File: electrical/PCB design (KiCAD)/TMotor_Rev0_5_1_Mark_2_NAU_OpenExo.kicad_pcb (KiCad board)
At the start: 2 copper layers, 89.3 x 79.4 mm, 85 parts, among them J1 Conn_01x07_Pin, J10 XT30PW-F, J11 XT30PW-F, J12 XT30PW-F, J2 Conn_01x04_Pin, J3 Conn_01x02_Pin, J4 Conn_01x02_Pin, J5 Conn_01x02_Pin, J6 Conn_01x02_Pin, J7 Conn_01x03_Pin, J8 XT30PW-F, J9 XT30PW-F, U1 TXU0104PWR, U10 DEV-16771, U2 TXU0304-Q1, U3 INA125U, U4 INA125U, U5 SN65HVD230DR, U6 INA125U, U7 INA125U

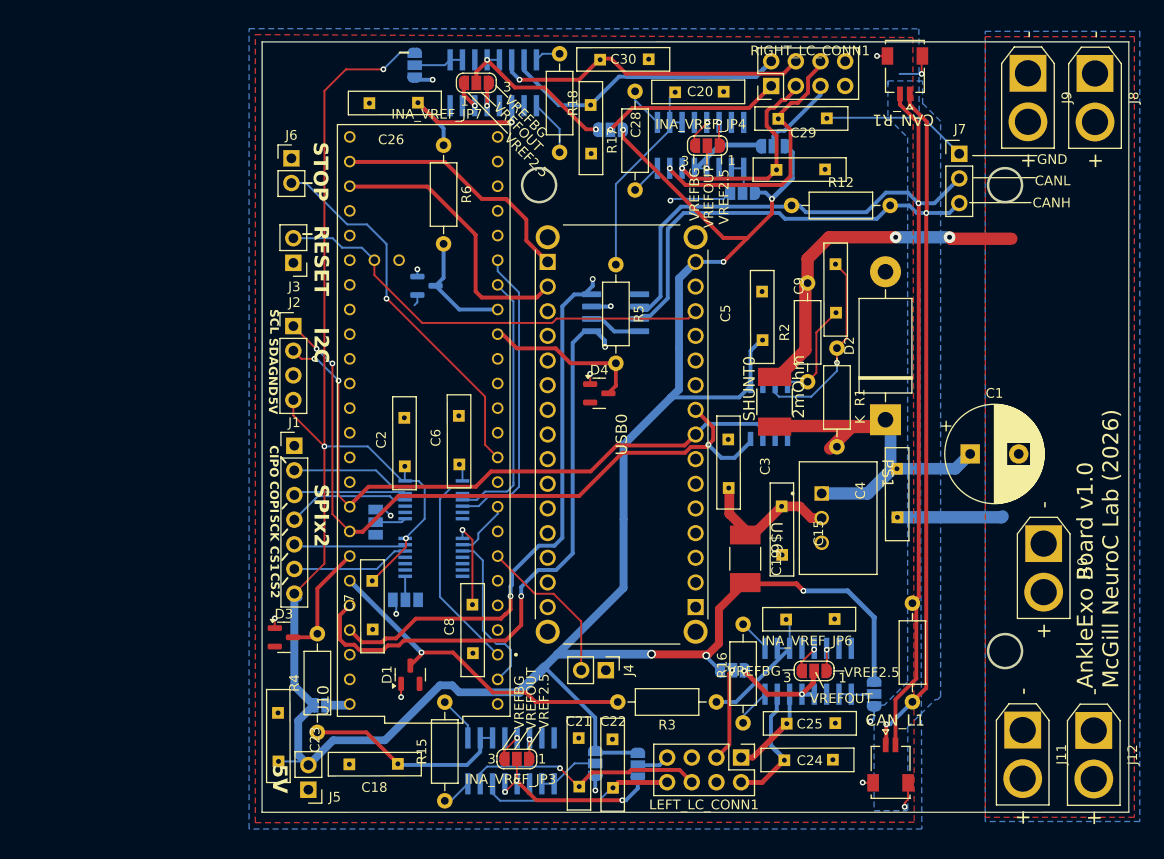
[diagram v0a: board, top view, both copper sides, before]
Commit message: documentation update for my 10 days leave ; documentation for first time teensy setup on Arduino IDE ;  SW revamp to use HW versioning conditional compiling
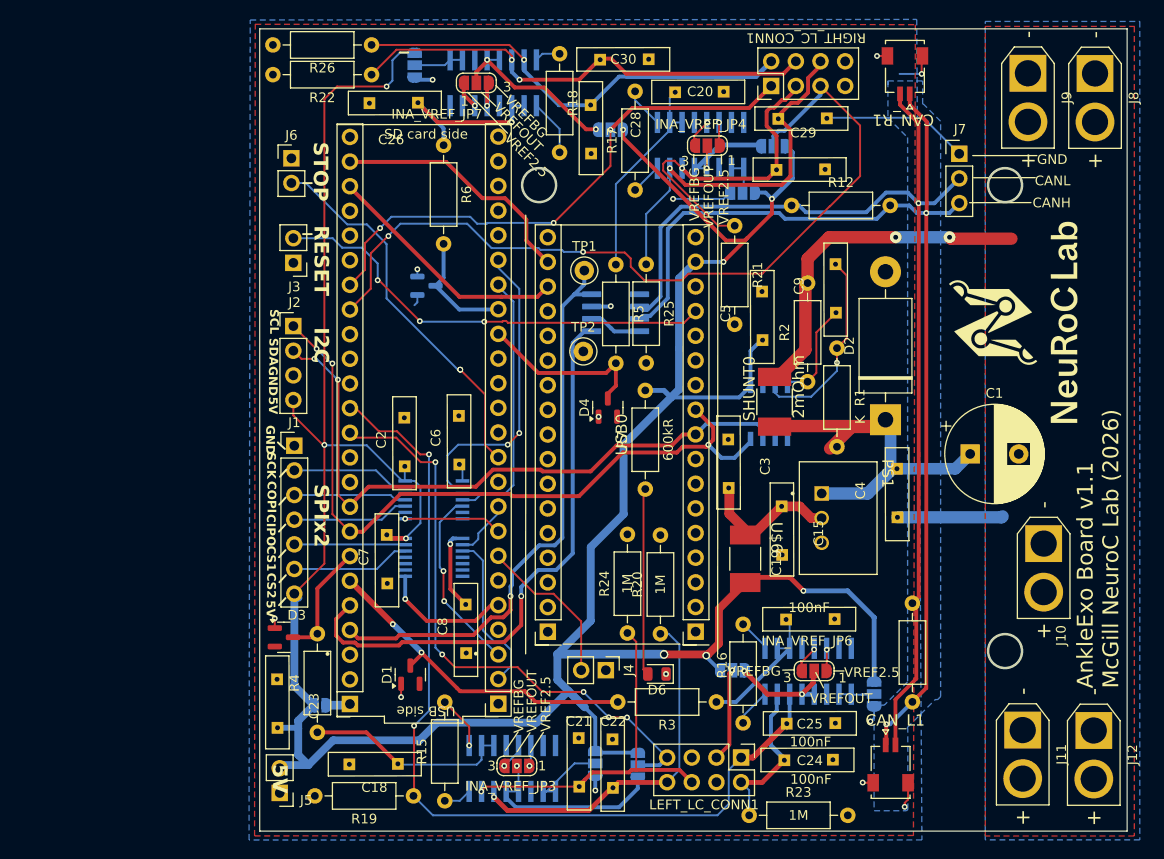
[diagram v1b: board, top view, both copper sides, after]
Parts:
- removed CSVoltageShifterOEJP1, SPIVoltageShifterOEJP1: SolderJumper_3_Open, Jumper:SolderJumper-3_P1.3mm_Open_Pad1.0x1.5mm
- added D6: LED, LED_SMD:LED_0805_2012Metric, F.Cu at (144.3, 130.4)
- added R19: 1M, Resistor_THT:R_Axial_DIN0207_L6.3mm_D2.5mm_P10.16mm_Horizontal, F.Cu at (119.2, 143.0)
- added R20: 1M, Resistor_THT:R_Axial_DIN0207_L6.3mm_D2.5mm_P10.16mm_Horizontal, F.Cu at (144.7, 126.3)
- added R21: 1M, Resistor_THT:R_Axial_DIN0207_L6.3mm_D2.5mm_P10.16mm_Horizontal, F.Cu at (152.3, 84.3)
- added R22: 1M, Resistor_THT:R_Axial_DIN0207_L6.3mm_D2.5mm_P10.16mm_Horizontal, F.Cu at (114.9, 68.7)
- added R23: 1M, Resistor_THT:R_Axial_DIN0207_L6.3mm_D2.5mm_P10.16mm_Horizontal, F.Cu at (153.8, 145.0)
- added R24: 1M, Resistor_THT:R_Axial_DIN0207_L6.3mm_D2.5mm_P10.16mm_Horizontal, F.Cu at (141.3, 126.2)
- added R25: 1M, Resistor_THT:R_Axial_DIN0207_L6.3mm_D2.5mm_P10.16mm_Horizontal, F.Cu at (143.2, 88.2)
- added R26: 1M, Resistor_THT:R_Axial_DIN0207_L6.3mm_D2.5mm_P10.16mm_Horizontal, F.Cu at (114.9, 65.6)
- added R7: 600kR, Resistor_THT:R_Axial_DIN0207_L6.3mm_D2.5mm_P10.16mm_Horizontal, F.Cu at (143.1, 111.4)
- added TP1: TestPoint, TestPoint:TestPoint_Keystone_5000-5004_Miniature, F.Cu at (136.8, 88.9)
- added TP2: TestPoint, TestPoint:TestPoint_Keystone_5000-5004_Miniature, F.Cu at (136.8, 97.2)
- G***: moved to F.Cu
- R15, R16, R17, R18: value 470R -> 10R
- moved G*** 45.7 mm to (181.4, 94.3)
- moved C7 4.97 mm to (116.5, 120.8)
- moved C23 3.47 mm to (105.3, 131.2)
- moved J5 2.97 mm to (105.5, 142.7)
- moved D4 1.72 mm to (139.3, 103.0), turned to 90 degrees
- moved U3 0.80 mm to (129.4, 140.2)
- moved INA_VREF_JP3 0.71 mm to (129.9, 139.9)
- moved C8 0.70 mm to (124.6, 128.0)
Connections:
- net Net-(J1-Pin_2) renamed /MCUs/SCK_5v
- C25 pad 1: /Load cells/Left LC Amplifier 2/Vbridge+ -> LEFT_AMP2_EXC
- INA_EXC_JP3 pad 2: /Load cells/Left LC  Amplifier 1/Vexcitation+ -> LEFT_AMP1_EXC
- INA_EXC_JP4 pad 2: /Load cells/Right LC  Amplifier 2/Vexcitation+ -> RIGHT_AMP2_EXC
- INA_EXC_JP7 pad 2: /Load cells/Right LC Amplifier 1/Vexcitation+ -> RIGHT_AMP1_EXC
- J1 pad 3: Net-(J1-Pin_3) -> /MCUs/COPI_5v
- J1 pad 4: Net-(J1-Pin_4) -> /MCUs/CIPO_5v
- LEFT_LC_CONN1 pad 1: /Load cells/Left LC Amplifier 2/Vbridge+ -> LEFT_AMP2_EXC
- LEFT_LC_CONN1 pad 7: /Load cells/Left LC  Amplifier 1/Vexcitation+ -> LEFT_AMP1_EXC
- RIGHT_LC_CONN1 pad 1: /Load cells/Right LC Amplifier 1/Vexcitation+ -> RIGHT_AMP1_EXC
- RIGHT_LC_CONN1 pad 5: /Load cells/Right LC  Amplifier 2/Vexcitation+ -> RIGHT_AMP2_EXC
- U1 pad 8: Net-(CSVoltageShifterOEJP1-C) -> /MCUs/OE2
- U10 pad 14: unconnected-(U10-A0-Pad14) -> LEFT_AMP2_EXC
- U10 pad 15: unconnected-(U10-A1-Pad15) -> LEFT_AMP1_EXC
- U10 pad 3: unconnected-(U10-LRCLK2-Pad3) -> /MCUs/OE2
- U10 pad 39: unconnected-(U10-A15-Pad39) -> RIGHT_AMP1_EXC
- U10 pad 40: unconnected-(U10-A16-Pad40) -> RIGHT_AMP2_EXC
- U10 pad 6: unconnected-(U10-OUT1D-Pad6) -> /MCUs/OE1
- U2 pad 10: unconnected-(U2-B4-Pad10) -> /MCUs/CIPO_5v
- U2 pad 11: Net-(J1-Pin_4) -> /MCUs/COPI_5v
- U2 pad 12: Net-(J1-Pin_3) -> unconnected-(U2-B2Y-Pad12)
- U2 pad 2: CIPO -> SCK1
- U2 pad 5: SCK1 -> CIPO
- U2 pad 8: Net-(SPIVoltageShifterOEJP1-C) -> /MCUs/OE1
- U6 pad 6: /Load cells/Left LC Amplifier 2/Vbridge+ -> LEFT_AMP2_EXC
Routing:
- net LEFT_AMP2_EXC: track 0.00 -> 95.0 mm, vias 0 -> 2
- net RIGHT_AMP2_EXC: track 0.00 -> 85.5 mm, vias 0 -> 2
- net LEFT_AMP1_EXC: track 0.00 -> 61.1 mm, vias 0 -> 5
- net RIGHT_AMP1_EXC: track 0.00 -> 56.4 mm, vias 0 -> 3
- net Net-(D6-A): track 0.00 -> 19.3 mm
- net /Load cells/Right LC Amplifier 1/Vexcitation+: track 18.4 -> 0.00 mm, vias 1 -> 0
- net /Load cells/Right LC Amplifier 1/Vbridge-: track 30.2 -> 46.5 mm, vias 0 -> 1
- net /Load cells/Right LC Amplifier 1/Vbridge+: track 33.0 -> 49.1 mm, vias 1 -> 2
- net /Load cells/Left LC  Amplifier 1/Vbridge+: track 21.5 -> 37.3 mm, vias 0 -> 1
- net /MCUs/OE2: track 0.00 -> 13.6 mm, vias 0 -> 1
- net /Load cells/Right LC  Amplifier 2/Vbridge+: track 21.4 -> 34.3 mm
- net Net-(J1-Pin_4): track 12.8 -> 0.00 mm
- net /Load cells/Left LC  Amplifier 1/Vbridge-: track 26.2 -> 38.7 mm
- net /MCUs/COPI_5v: track 0.00 -> 12.1 mm
- net /MCUs/CIPO_5v: track 0.00 -> 12.0 mm
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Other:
- board size 89.3 x 79.4 mm -> 89.4 x 82.6 mm
- board text added: "AnkleExo Board v1.1 McGill NeuroC Lab (2026)"
- board text removed: "AnkleExo Board v1.0 McGill NeuroC Lab (2026)"

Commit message: some modifications on the kicad
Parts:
- moved G*** 0.77 mm to (180.6, 94.3)
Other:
- board text added: "AnkleExo Board v1.0.1 McGill NeuroC Lab (2026)"
- board text removed: "AnkleExo Board v1.1 McGill NeuroC Lab (2026)"

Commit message: kicad update
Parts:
- added J13: TFM-107-01-L-D-WT, ISDF connector:SAMTEC_TFM-107-01-L-D-WT, F.Cu at (86.5, 123.1)

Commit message: PCB version v1.1.0 design+documentation
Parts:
- removed J13: TFM-107-01-L-D-WT, ISDF connector:SAMTEC_TFM-107-01-L-D-WT
- removed USB0: ABX00028, TMotor_Rev0_5_1_Mark_2_NAU_OpenExo:ABX00028
- added A1: Arduino_Nano_33_BLE_Sense_R2_Socket, PCM_arduino-library:Arduino_Nano_Every_Socket, F.Cu at (140.7, 127.4)
- moved D3 36.4 mm to (139.6, 113.1)
- moved R4 30.4 mm to (139.5, 133.3), turned to 0 degrees
- moved D1 23.5 mm to (140.6, 121.3), turned to -90 degrees
- moved R3 20.1 mm to (167.1, 122.0)
- moved LEFT_LC_CONN1 8.03 mm to (145.4, 141.6), turned to 90 degrees
- moved D4 1.59 mm to (138.5, 101.6)
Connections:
- C25 pad 1: LEFT_AMP2_EXC -> /Load cells/Left LC Amplifier 2/Vbridge+
- D1 pad 3: LEFT_LC_AMP2 -> L2_LC_N
- D3 pad 3: LEFT_LC_AMP1 -> L1_LC_N
- D4 pad 3: RIGHT_LC_AMP2 -> R2_LC_N
- D5 pad 3: RIGHT_LC_AMP1 -> R1_LC_N
- INA_EXC_JP3 pad 2: LEFT_AMP1_EXC -> L1_LC_P
- INA_EXC_JP4 pad 2: RIGHT_AMP2_EXC -> R2_LC_P
- INA_EXC_JP6 pad 2: /Load cells/Left LC Amplifier 2/Vexcitation+ -> L2_LC_P
- INA_EXC_JP7 pad 2: RIGHT_AMP1_EXC -> R1_LC_P
- LEFT_LC_CONN1 pad 1: LEFT_AMP2_EXC -> /Load cells/Left LC Amplifier 2/Vbridge+
- LEFT_LC_CONN1 pad 2: /Load cells/Left LC Amplifier 2/Vbridge- -> GND
- LEFT_LC_CONN1 pad 3: /Load cells/Left LC Amplifier 2/Vexcitation+ -> /Load cells/Left LC Amplifier 2/Vbridge-
- LEFT_LC_CONN1 pad 4: GND -> +5V
- LEFT_LC_CONN1 pad 5: GND -> +5V
- LEFT_LC_CONN1 pad 7: LEFT_AMP1_EXC -> GND
- R19 pad 1: LEFT_AMP2_EXC -> /Load cells/Left LC Amplifier 2/Vbridge+
- R3 pad 2: LEFT_LC_AMP2 -> L2_LC_N
- R4 pad 2: LEFT_LC_AMP1 -> L1_LC_N
- R5 pad 2: RIGHT_LC_AMP2 -> R2_LC_N
- R6 pad 2: RIGHT_LC_AMP1 -> R1_LC_N
- RIGHT_LC_CONN1 pad 1: RIGHT_AMP1_EXC -> /Load cells/Right LC  Amplifier 2/Vbridge+
- RIGHT_LC_CONN1 pad 2: /Load cells/Right LC Amplifier 1/Vbridge- -> GND
- RIGHT_LC_CONN1 pad 3: /Load cells/Right LC  Amplifier 2/Vbridge+ -> /Load cells/Right LC  Amplifier 2/Vbridge-
- RIGHT_LC_CONN1 pad 4: /Load cells/Right LC Amplifier 1/Vbridge+ -> +5V
- RIGHT_LC_CONN1 pad 5: RIGHT_AMP2_EXC -> +5V
- RIGHT_LC_CONN1 pad 6: /Load cells/Right LC  Amplifier 2/Vbridge- -> /Load cells/Right LC Amplifier 1/Vbridge-
- RIGHT_LC_CONN1 pad 8: GND -> /Load cells/Right LC Amplifier 1/Vbridge+
- U10 pad 14: LEFT_AMP2_EXC -> unconnected-(U10-A0-Pad14)
- U10 pad 15: LEFT_AMP1_EXC -> unconnected-(U10-A1-Pad15)
- U10 pad 18: SDA -> unconnected-(U10-A4-Pad18)
- U10 pad 19: SCL -> unconnected-(U10-A5-Pad19)
- U10 pad 20: LEFT_LC_AMP1 -> unconnected-(U10-A6-Pad20)
- U10 pad 21: LEFT_LC_AMP2 -> unconnected-(U10-A7-Pad21)
- U10 pad 24: RIGHT_LC_AMP2 -> unconnected-(U10-A10-Pad24)
- U10 pad 25: RIGHT_LC_AMP1 -> unconnected-(U10-A11-Pad25)
- U10 pad 39: RIGHT_AMP1_EXC -> unconnected-(U10-A15-Pad39)
- U10 pad 40: RIGHT_AMP2_EXC -> unconnected-(U10-A16-Pad40)
- U6 pad 6: LEFT_AMP2_EXC -> /Load cells/Left LC Amplifier 2/Vbridge+
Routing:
- net LEFT_AMP2_EXC: track 95.0 -> 0.00 mm, vias 2 -> 0
- net RIGHT_AMP2_EXC: track 85.5 -> 0.00 mm, vias 2 -> 0
- net LEFT_AMP1_EXC: track 61.1 -> 0.00 mm, vias 5 -> 0
- net R1_LC_P: track 0.00 -> 58.8 mm, vias 0 -> 3
- net RIGHT_AMP1_EXC: track 56.4 -> 0.00 mm, vias 3 -> 0
- net /Load cells/Left LC Amplifier 2/Vbridge+: track 0.00 -> 51.7 mm
- net R2_LC_P: track 0.00 -> 50.2 mm, vias 0 -> 1
- net R1_LC_N: track 0.00 -> 42.7 mm, vias 0 -> 1
- net L1_LC_P: track 0.00 -> 36.6 mm, vias 0 -> 3
- net L1_LC_N: track 0.00 -> 35.7 mm, vias 0 -> 2
- net LEFT_LC_AMP2: track 34.6 -> 0.00 mm, vias 2 -> 0
- net L2_LC_P: track 0.00 -> 31.5 mm
- net +5V: track 315.7 -> 343.3 mm
- net L2_LC_N: track 0.00 -> 26.1 mm, vias 0 -> 1
- net RIGHT_LC_AMP2: track 17.8 -> 0.00 mm
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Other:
- board text added: "AnkleExo Board v1.1.0 McGill NeuroC Lab (2026)"
- board text removed: "AnkleExo Board v1.0.1 McGill NeuroC Lab (2026)"

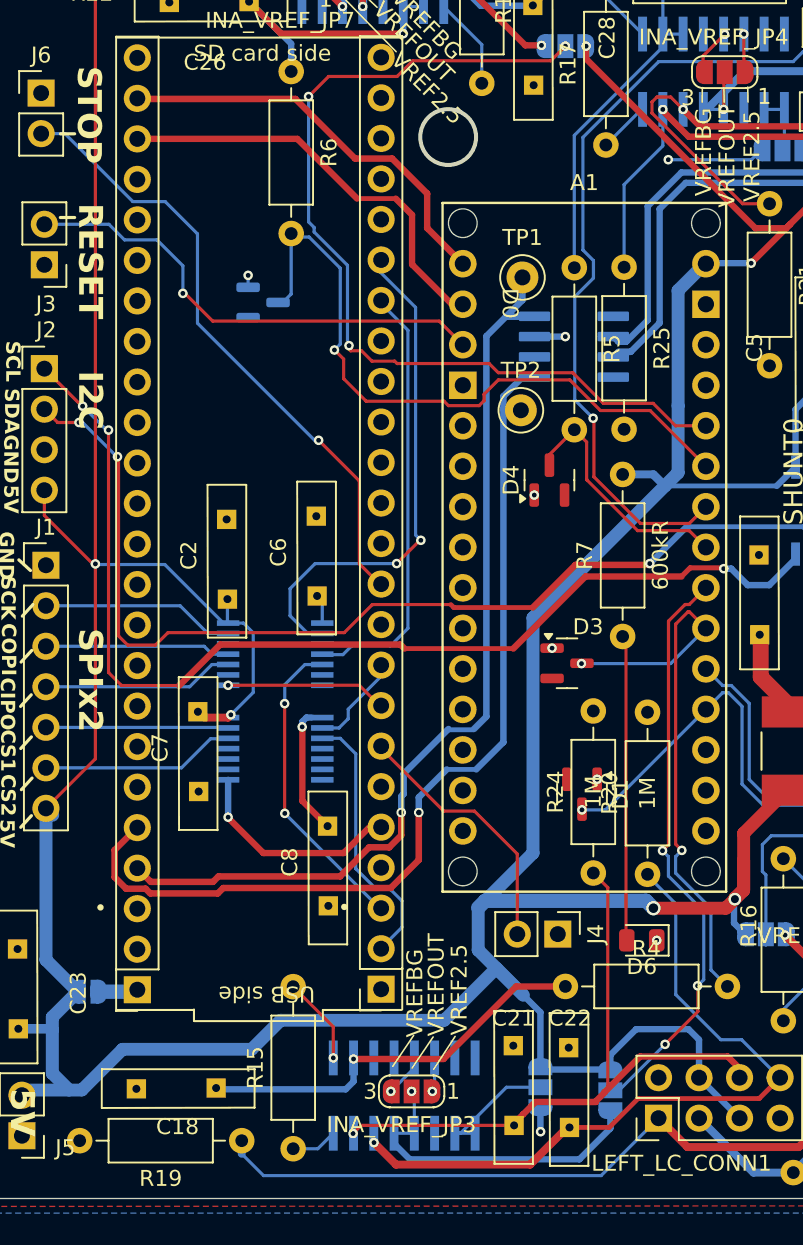
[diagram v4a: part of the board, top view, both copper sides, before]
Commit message: integration of Encoders/LC/motors into main.cpp.
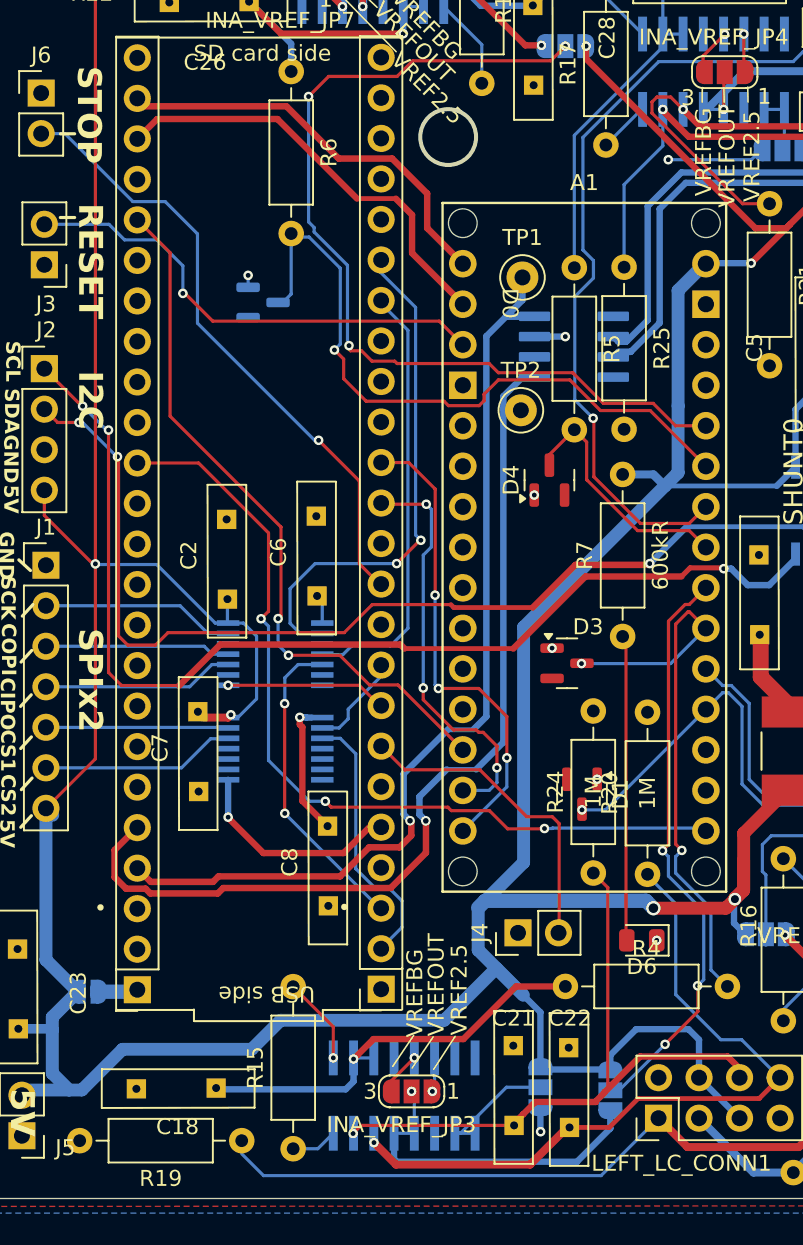
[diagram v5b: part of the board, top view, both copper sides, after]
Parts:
- moved J4 2.50 mm to (136.6, 130.0), turned to 90 degrees
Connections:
- A1 pad D10: unconnected-(A1-PadD10) -> /MCUs/NANO_CS
- A1 pad D11: unconnected-(A1-D11_MOSI-PadD11) -> /MCUs/NANO_MOSI
- A1 pad D12: unconnected-(A1-D12_MISO-PadD12) -> /MCUs/NANO_MISO
- A1 pad D13: unconnected-(A1-D13_SCK-PadD13) -> /MCUs/NANO_SCK
- U10 pad 11: unconnected-(U10-MOSI-Pad11) -> /MCUs/NANO_MOSI
- U10 pad 12: unconnected-(U10-MISO-Pad12) -> /MCUs/NANO_MISO
- U10 pad 13: unconnected-(U10-SCK-Pad13) -> /MCUs/NANO_SCK
- U10 pad 37: unconnected-(U10-CS3-Pad37) -> /MCUs/NANO_CS
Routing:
- net /MCUs/NANO_SCK: track 0.00 -> 54.0 mm, vias 0 -> 3
- net /MCUs/NANO_CS: track 0.00 -> 44.8 mm, vias 0 -> 2
- net /MCUs/NANO_MISO: track 0.00 -> 30.0 mm, vias 0 -> 3
- net /MCUs/NANO_MOSI: track 0.00 -> 26.0 mm, vias 0 -> 3
- net SYNC_DEFAULT: track 16.4 -> 20.1 mm
- net /Load cells/Left LC Amplifier 2/Vbridge+: track 51.7 -> 50.9 mm
- net Net-(INA_VREF_JP3-B): track 2.71 -> 3.51 mm
- net CANRX: track 59.0 -> 59.8 mm
- net Net-(INA_EXC_JP3-B): track 20.5 -> 21.2 mm
- net /MCUs/NANO_RX: track 27.0 -> 27.6 mm
- net +5V: track 343.3 -> 343.8 mm
